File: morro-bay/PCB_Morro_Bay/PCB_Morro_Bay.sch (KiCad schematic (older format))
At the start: 31 parts, among them J1 USB_B, J2 Conn_01x02, U1 MCP2515-xSO, U2 MIC5504-3.3YM5, U3 SN65HVD232, U4 ATSAMD21J18A-AU

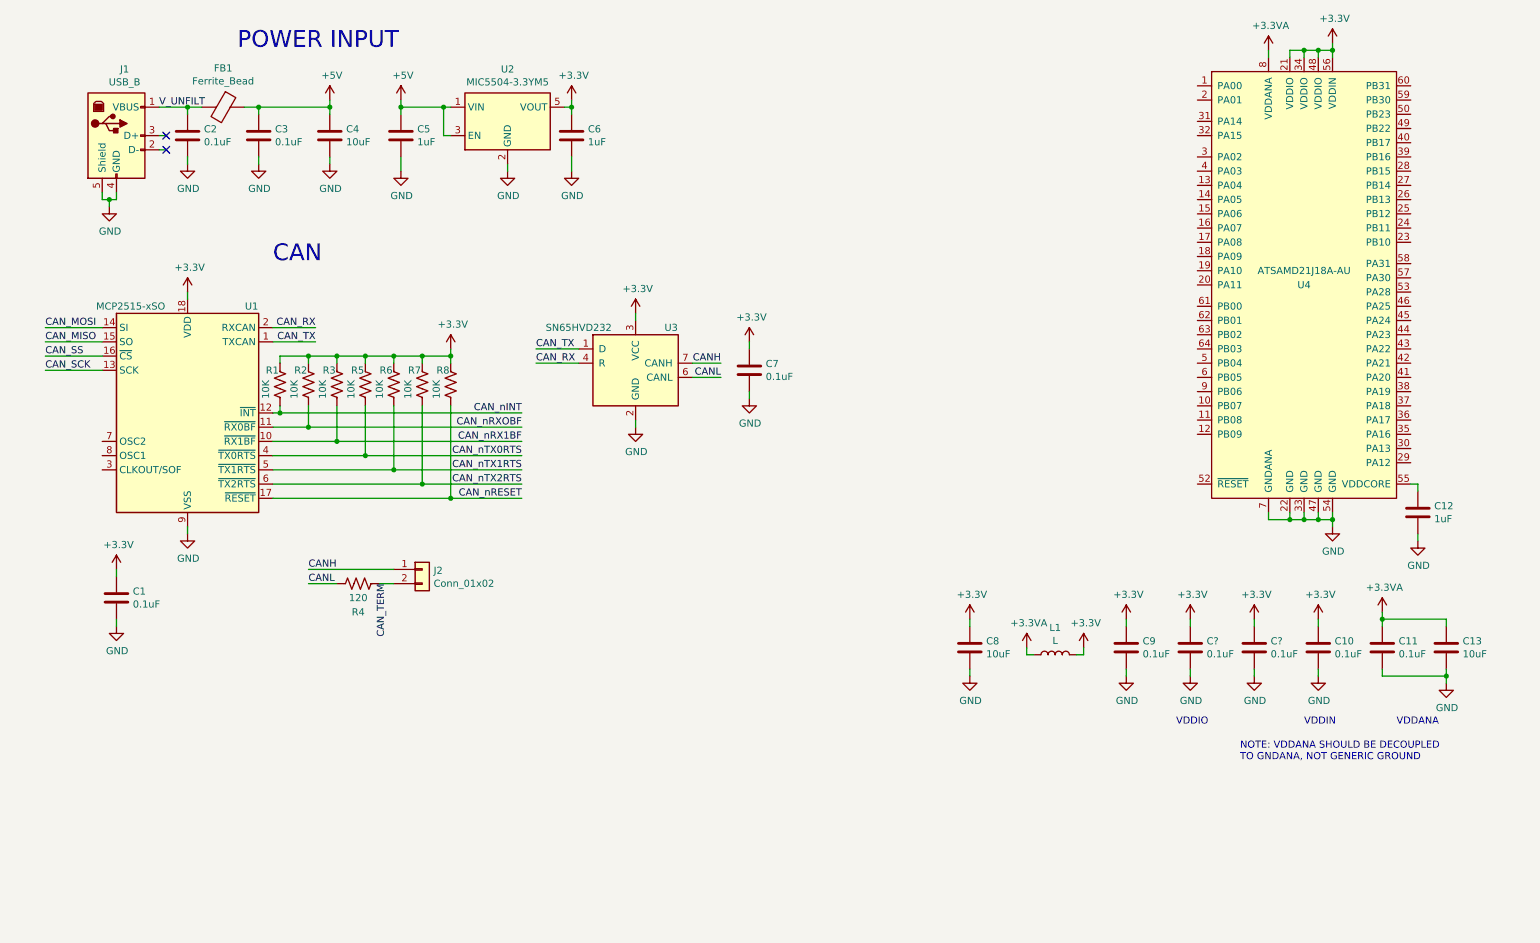
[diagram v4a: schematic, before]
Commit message: Add crystals
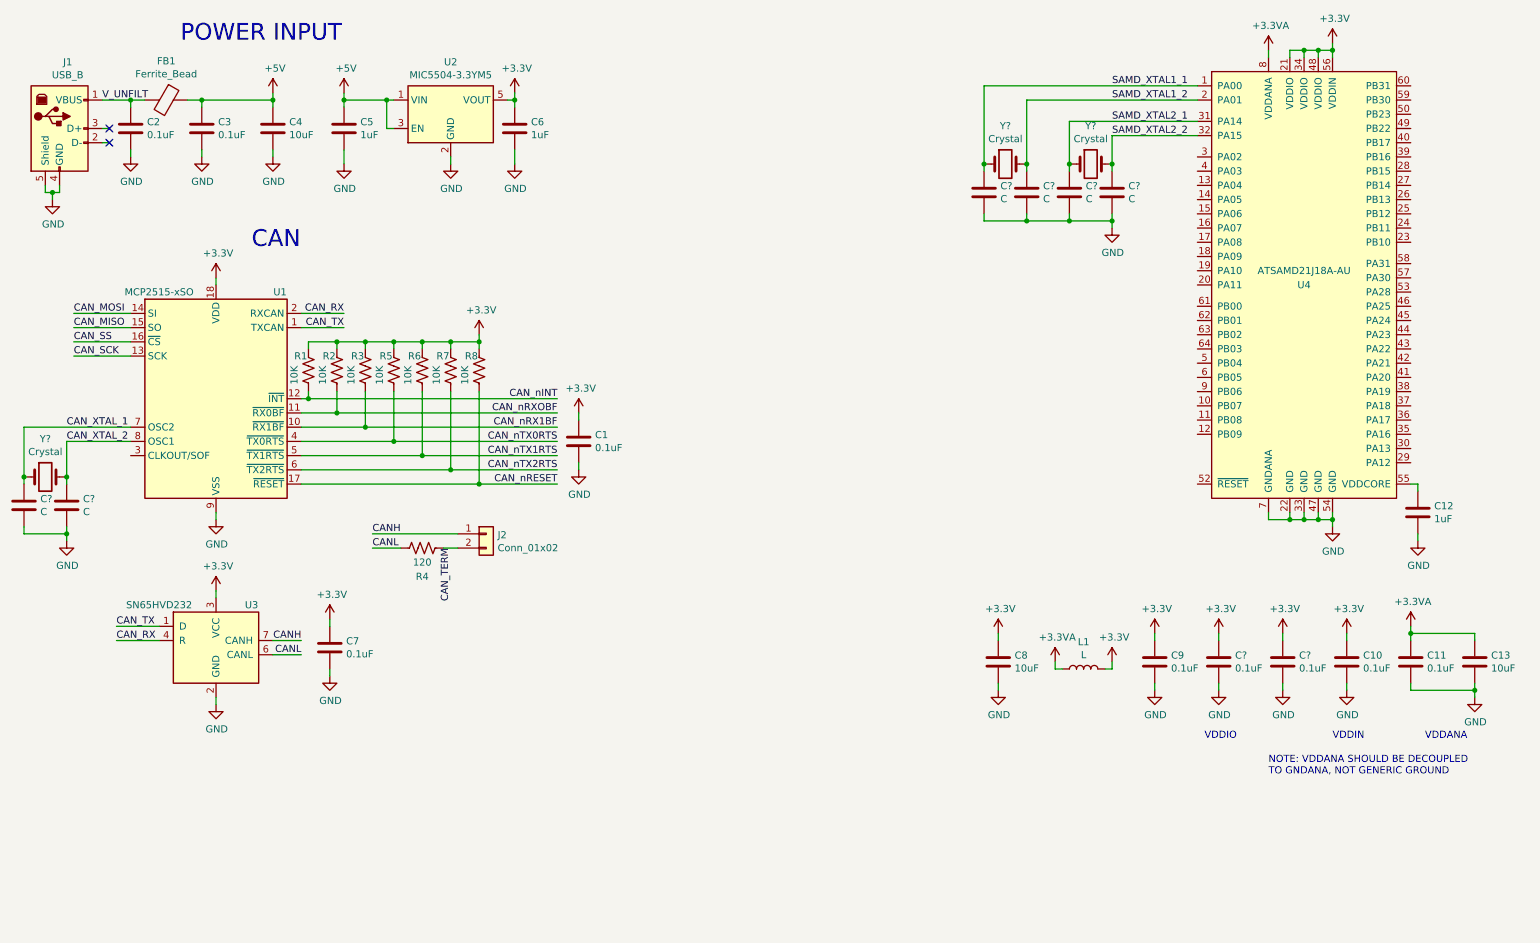
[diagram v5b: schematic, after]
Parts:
- added C? (x6): C, symbol Device:C
- added Y? (x3): Crystal, symbol Device:Crystal
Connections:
- net GND: now also C?.2, C?.2, C?.2, C?.2, C?.2, C?.2
- net CAN_XTAL_1: now reaches U1.7 (OSC2)
- net CAN_XTAL_1: now also C?.1, Y?.1
- net CAN_XTAL_2: now reaches U1.8 (OSC1)
- net CAN_XTAL_2: now also C?.1, Y?.2
- net SAMD_XTAL1_1: now reaches U4.1 (PA00)
- net SAMD_XTAL1_1: now also C?.1, Y?.1
- net SAMD_XTAL1_2: now reaches U4.2 (PA01)
- net SAMD_XTAL1_2: now also C?.1, Y?.2
- net SAMD_XTAL2_1: now reaches U4.31 (PA14)
- net SAMD_XTAL2_1: now also C?.1, Y?.1
- net SAMD_XTAL2_2: now reaches U4.32 (PA15)
- net SAMD_XTAL2_2: now also C?.1, Y?.2
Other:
- moved on the sheet: C1, C10, C11, C13, C2, C3, C4, C5, C6, C7, C8, C9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

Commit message: Add analog resistor dividers
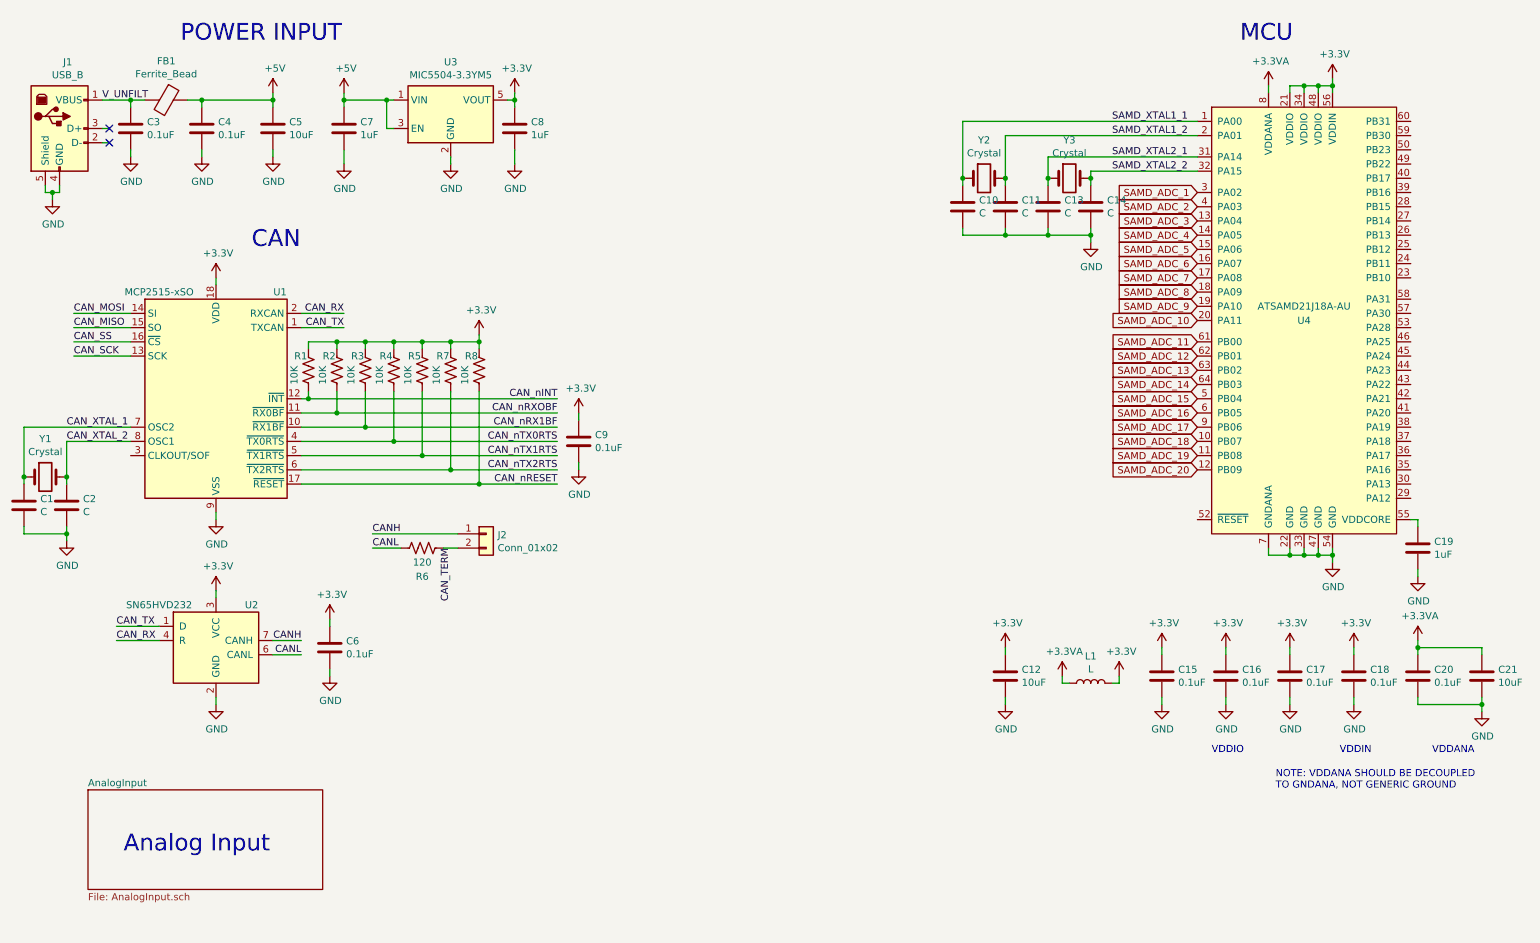
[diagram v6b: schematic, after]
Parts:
- gave numbers to parts that had none: 11
- renumbered C8 to C12, C9 to C15, C10 to C18, C12 to C19, C11 to C20, C13 to C21, C2 to C3, C3 to C4, C4 to C5, C7 to C6, C5 to C7, C6 to C8, C1 to C9, R5 to R4, R6 to R5, R4 to R6, U3 to U2, U2 to U3
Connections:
- net SAMD_ADC_18: now reaches U4.10 (PB07)
- net SAMD_ADC_19: now reaches U4.11 (PB08)
- net SAMD_ADC_20: now reaches U4.12 (PB09)
- net SAMD_ADC_3: now reaches U4.13 (PA04)
- net SAMD_ADC_4: now reaches U4.14 (PA05)
- net SAMD_ADC_5: now reaches U4.15 (PA06)
- net SAMD_ADC_6: now reaches U4.16 (PA07)
- net SAMD_ADC_7: now reaches U4.17 (PA08)
- net SAMD_ADC_8: now reaches U4.18 (PA09)
- net SAMD_ADC_9: now reaches U4.19 (PA10)
- net SAMD_ADC_10: now reaches U4.20 (PA11)
- net SAMD_ADC_1: now reaches U4.3 (PA02)
- net SAMD_ADC_2: now reaches U4.4 (PA03)
- net SAMD_ADC_15: now reaches U4.5 (PB04)
- net SAMD_ADC_16: now reaches U4.6 (PB05)
- net SAMD_ADC_11: now reaches U4.61 (PB00)
- net SAMD_ADC_12: now reaches U4.62 (PB01)
- net SAMD_ADC_13: now reaches U4.63 (PB02)
- net SAMD_ADC_14: now reaches U4.64 (PB03)
- net SAMD_ADC_17: now reaches U4.9 (PB06)
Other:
- note added: "Analog Input"
- note added: "MCU"
- moved on the sheet: C10, C11, C12, C13, C14, C15, C16, C17, C18, C19, C20, C21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

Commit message: Work on analog inputs
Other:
- moved on the sheet: C10, C11, C13, C14, Y2, Y3

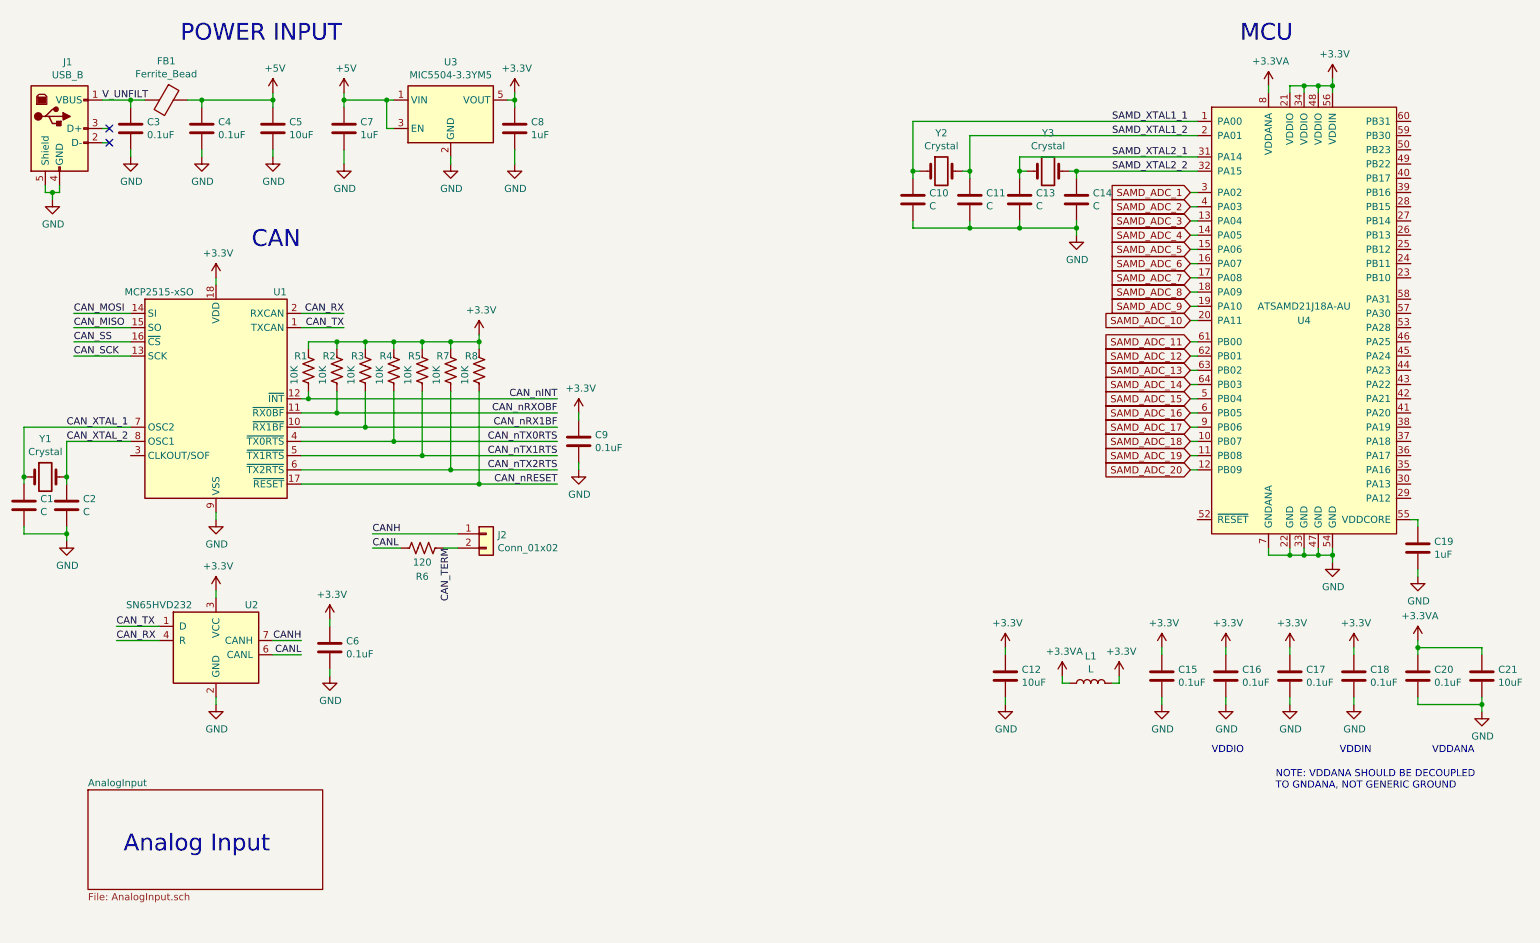
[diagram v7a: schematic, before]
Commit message: Work on analog inputs and pin naming
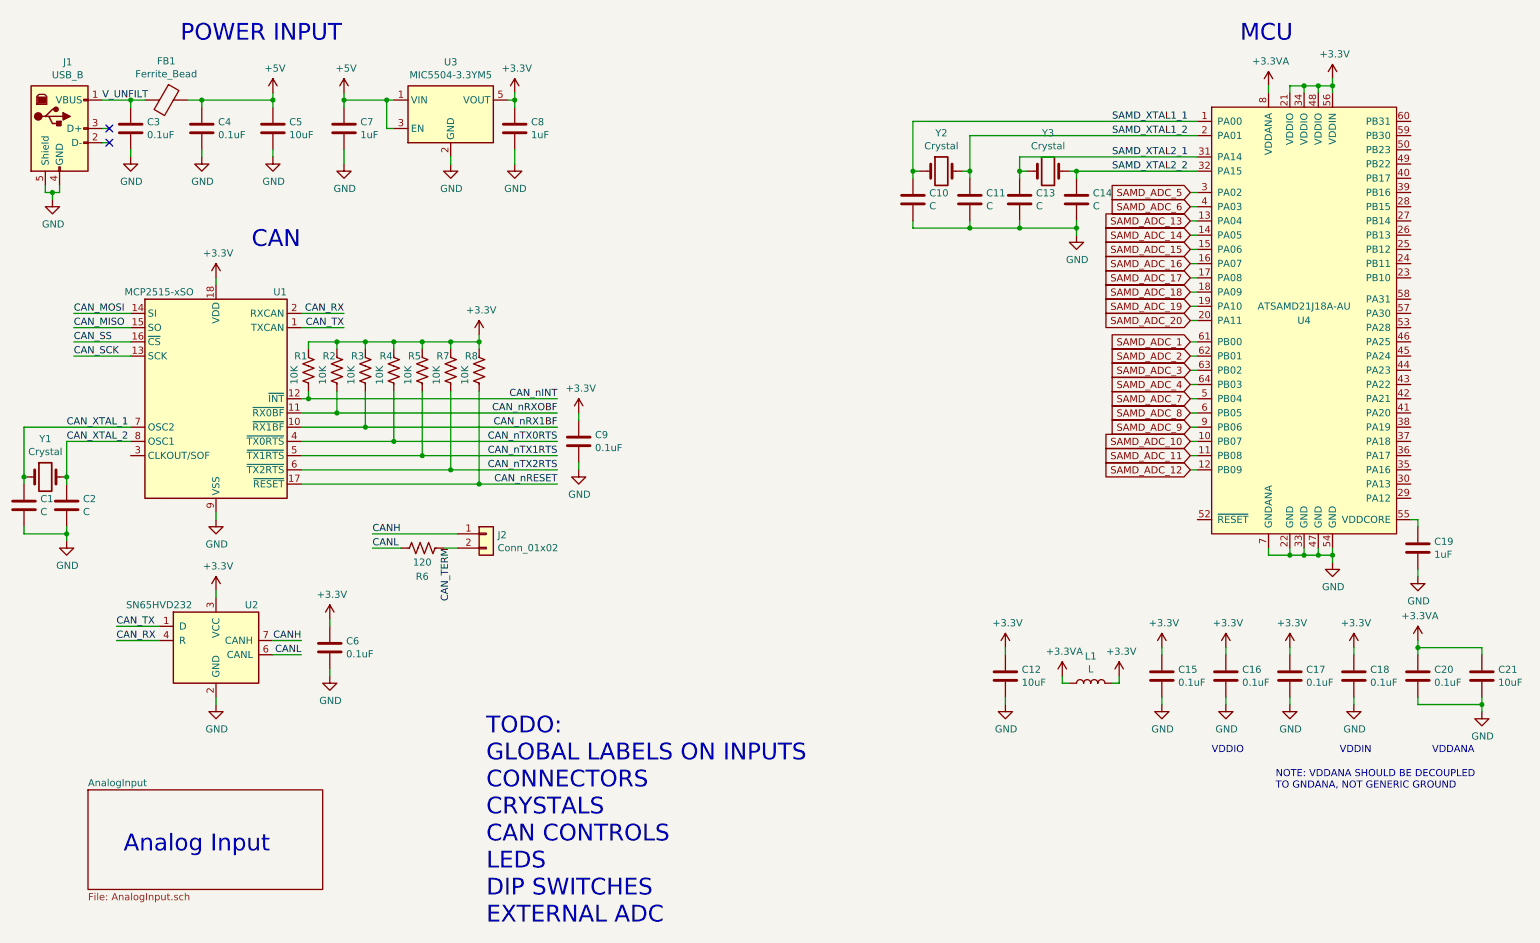
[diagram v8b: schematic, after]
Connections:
- net SAMD_ADC_1: now also U4.61 (PB00); no longer U4.3 (PA02)
- net SAMD_ADC_10: now also U4.10 (PB07); no longer U4.20 (PA11)
- net SAMD_ADC_11: now also U4.11 (PB08); no longer U4.61 (PB00)
- net SAMD_ADC_12: now also U4.12 (PB09); no longer U4.62 (PB01)
- net SAMD_ADC_13: now also U4.13 (PA04); no longer U4.63 (PB02)
- net SAMD_ADC_14: now also U4.14 (PA05); no longer U4.64 (PB03)
- net SAMD_ADC_15: now also U4.15 (PA06); no longer U4.5 (PB04)
- net SAMD_ADC_16: now also U4.16 (PA07); no longer U4.6 (PB05)
- net SAMD_ADC_17: now also U4.17 (PA08); no longer U4.9 (PB06)
- net SAMD_ADC_18: now also U4.18 (PA09); no longer U4.10 (PB07)
- net SAMD_ADC_19: now also U4.19 (PA10); no longer U4.11 (PB08)
- net SAMD_ADC_2: now also U4.62 (PB01); no longer U4.4 (PA03)
- net SAMD_ADC_20: now also U4.20 (PA11); no longer U4.12 (PB09)
- net SAMD_ADC_3: now also U4.63 (PB02); no longer U4.13 (PA04)
- net SAMD_ADC_4: now also U4.64 (PB03); no longer U4.14 (PA05)
- net SAMD_ADC_5: now also U4.3 (PA02); no longer U4.15 (PA06)
- net SAMD_ADC_6: now also U4.4 (PA03); no longer U4.16 (PA07)
- net SAMD_ADC_7: now also U4.5 (PB04); no longer U4.17 (PA08)
- net SAMD_ADC_8: now also U4.6 (PB05); no longer U4.18 (PA09)
- net SAMD_ADC_9: now also U4.9 (PB06); no longer U4.19 (PA10)
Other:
- note added: "TODO:\nGLOBAL LABELS ON INPUTS\nCONNECTORS\nCRYSTALS\nCAN CONTROLS\nLEDS\nDIP SWITCHES\nEXTERNAL ADC"
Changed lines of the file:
@@
 Text Notes 1350 6450 0    118  ~ 0
 Analog Input
+Text GLabel 8850 2850 0    50   Input ~ 0
+SAMD_ADC_1
+Text GLabel 8850 2950 0    50   Input ~ 0
+SAMD_ADC_2
+Text GLabel 8850 3050 0    50   Input ~ 0
+SAMD_ADC_3
+Text GLabel 8850 3150 0    50   Input ~ 0
+SAMD_ADC_4
 Text GLabel 8850 1800 0    50   Input ~ 0
-SAMD_ADC_1
+SAMD_ADC_5
 Text GLabel 8850 1900 0    50   Input ~ 0
-SAMD_ADC_2
+SAMD_ADC_6
+Text GLabel 8850 3250 0    50   Input ~ 0
+SAMD_ADC_7
+Text GLabel 8850 3350 0    50   Input ~ 0
+SAMD_ADC_8
+Text GLabel 8850 3450 0    50   Input ~ 0
+SAMD_ADC_9
+Text GLabel 8850 3550 0    50   Input ~ 0
+SAMD_ADC_10
+Text GLabel 8850 3650 0    50   Input ~ 0
+SAMD_ADC_11
+Text GLabel 8850 3750 0    50   Input ~ 0
+SAMD_ADC_12
 Text GLabel 8850 2000 0    50   Input ~ 0
-SAMD_ADC_3
+SAMD_ADC_13
 Text GLabel 8850 2100 0    50   Input ~ 0
-SAMD_ADC_4
+SAMD_ADC_14
 Text GLabel 8850 2200 0    50   Input ~ 0
-SAMD_ADC_5
+SAMD_ADC_15
 Text GLabel 8850 2300 0    50   Input ~ 0
-SAMD_ADC_6
+SAMD_ADC_16
 Text GLabel 8850 2400 0    50   Input ~ 0
-SAMD_ADC_7
+SAMD_ADC_17
 Text GLabel 8850 2500 0    50   Input ~ 0
-SAMD_ADC_8
+SAMD_ADC_18
 Text GLabel 8850 2600 0    50   Input ~ 0
-SAMD_ADC_9
-Text GLabel 8850 2700 0    50   Input ~ 0
-SAMD_ADC_10
-Text GLabel 8850 2850 0    50   Input ~ 0
-SAMD_ADC_11
-Text GLabel 8850 2950 0    50   Input ~ 0
-SAMD_ADC_12
-Text GLabel 8850 3050 0    50   Input ~ 0
-SAMD_ADC_13
-Text GLabel 8850 3150 0    50   Input ~ 0
-SAMD_ADC_14
-Text GLabel 8850 3250 0    50   Input ~ 0
-SAMD_ADC_15
-Text GLabel 8850 3350 0    50   Input ~ 0
-SAMD_ADC_16
-Text GLabel 8850 3450 0    50   Input ~ 0
-SAMD_ADC_17
-Text GLabel 8850 3550 0    50   Input ~ 0
-SAMD_ADC_18
-Text GLabel 8850 3650 0    50   Input ~ 0
 SAMD_ADC_19
 Wire Wire Line
@@
 Wire Wire Line
 	2600 3250 2650 3250
-Text GLabel 8850 3750 0    50   Input ~ 0
+Text GLabel 8850 2700 0    50   Input ~ 0
 SAMD_ADC_20
 Wire Wire Line
@@
 Wire Wire Line
 	8050 1650 8050 1700
+Text Notes 3900 6950 0    118  ~ 0
+TODO:\nGLOBAL LABELS ON INPUTS\nCONNECTORS\nCRYSTALS\nCAN CONTROLS\nLEDS\nDIP SWITCHES\nEXTERNAL ADC
 $EndSCHEMATC
